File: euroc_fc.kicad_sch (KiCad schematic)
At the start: 147 parts, among them J1 Micro-Fit, J10 USB_C_Receptacle_USB2.0, J11 SWD Header, J2 Micro-Fit, J3 Micro-Fit, J4 SMA, J5 JST-GH, J6 JST-GH, J7 JST-GH, J9 Micro_SD_Card_Det, Q1 DMN2056U, Q2 AOSP21321, Q3 DMN2056U, Q4 AOSP21321, Q5 DMN2056U, SW1 EVQ-PUC02K, SW2 EVQ-PUC02K, U1 STM32F401RCT6, U10 Ai-Thinker-Ra-01, U11 W25Q256JVF, U12 MCP2517FD, U13 MCP2562-E-SN, U2 L7805, U3 L7805, U4 AZ1117I-3.3, U5 LSM6DSR, U6 H3LIS331DL, U7 MS5611-01BA, U8 LIS3MDL, U9 SAM-M8Q, Y1 25M, 18p, Y2 20M

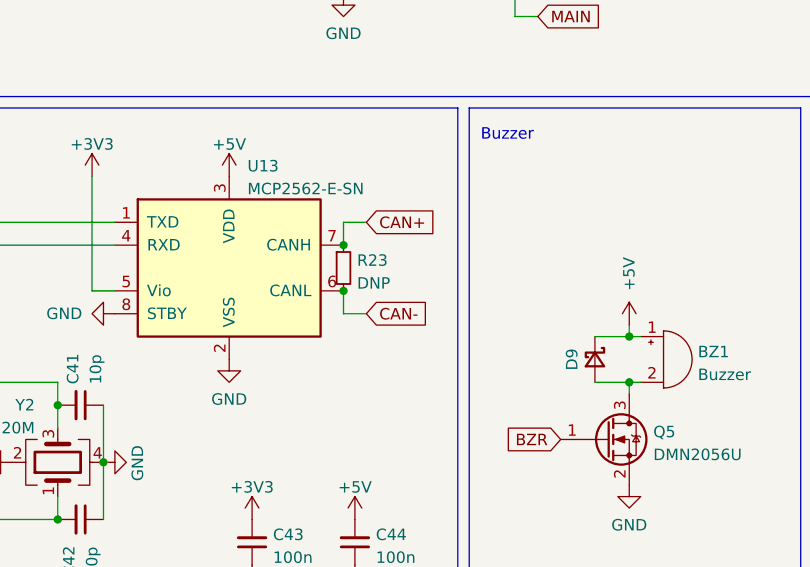
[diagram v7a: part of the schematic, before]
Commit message: Update BOM for rev. 2
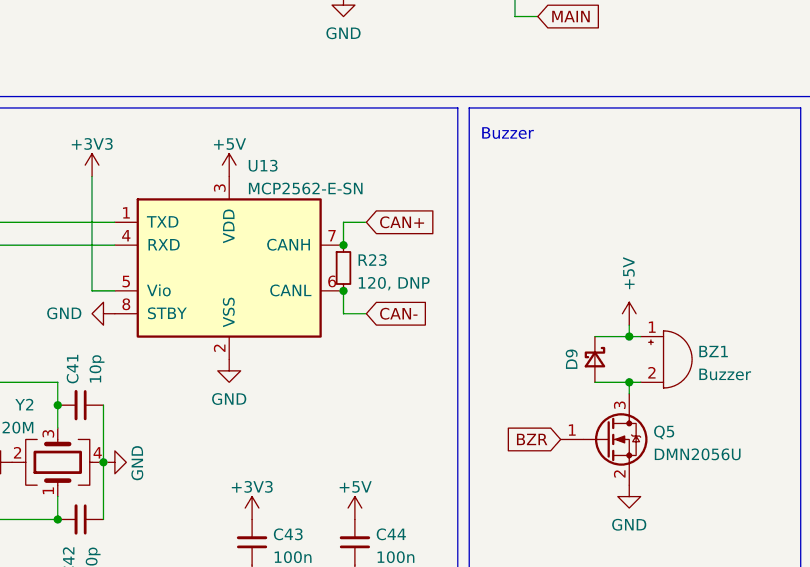
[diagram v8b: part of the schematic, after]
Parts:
- C41, C42: LCSC# (none) -> C1634; Manufacturer (none) -> Samsung Electro-Mechanics; Part# (none) -> CL10C100JB8NNNC
- J5, J6, J7: LCSC# (none) -> C189895; Manufacturer (none) -> JST; Part# (none) -> SM04B-GHS-TB
- R23: value DNP -> 120, DNP; LCSC# C22548 -> C114640; Part# RC0603FR-071KL -> RC0603FR-07120RL
- U11: LCSC# (none) -> C779876
- U12: DigiKey# (none) -> MCP2517FDT-H/SLCT-ND; Manufacturer (none) -> Microchip Technology; Part# (none) -> MCP2517FDT-H/SL
- U13: DigiKey# (none) -> MCP2562-H/SN; Manufacturer (none) -> Microchip Technology; Part# (none) -> MCP2562-H/SN
- U6: DigiKey# (none) -> 497-13903-1-ND; Manufacturer (none) -> STMicroelectronics; Part# (none) -> H3LIS331DLTR
- U8: DigiKey# (none) -> 497-13892-1-ND; LCSC# (none) -> C478483; Manufacturer (none) -> STMicroelectronics; Part# (none) -> LIS3MDLTR
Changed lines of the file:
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@@
       (effects (font (size 1.27 1.27)) hide)
     )
+    (property "Manufacturer" "Microchip Technology" (id 4) (at 173.99 148.59 0)
+      (effects (font (size 1.27 1.27)) hide)
+    )
+    (property "DigiKey#" "MCP2562-H/SN" (id 5) (at 173.99 148.59 0)
+      (effects (font (size 1.27 1.27)) hide)
+    )
+    (property "Part#" "MCP2562-H/SN" (id 6) (at 173.99 148.59 0)
+      (effects (font (size 1.27 1.27)) hide)
+    )
     (pin "1")
     (pin "2")
@@
       (effects (font (size 1.27 1.27)) (justify left))
     )
-    (property "Value" "DNP" (id 1) (at 188.1886 150.2922 0)
+    (property "Value" "120, DNP" (id 1) (at 188.1886 150.2922 0)
       (effects (font (size 1.27 1.27)) (justify left))
     )
@@
       (effects (font (size 1.27 1.27)) hide)
     )
-    (property "LCSC#" "C22548" (id 5) (at 186.69 148.59 0)
+    (property "LCSC#" "C114640" (id 5) (at 186.69 148.59 0)
       (effects (font (size 1.27 1.27)) hide)
     )
@@
       (effects (font (size 1.27 1.27)) hide)
     )
-    (property "Part#" "RC0603FR-071KL" (id 7) (at 186.69 148.59 0)
+    (property "Part#" "RC0603FR-07120RL" (id 7) (at 186.69 148.59 0)
       (effects (font (size 1.27 1.27)) hide)
     )
@@
       (effects (font (size 1.27 1.27)) hide)
     )
-    (property "LCSC#" "" (id 5) (at 157.48 176.53 0)
+    (property "LCSC#" "C1634" (id 5) (at 157.48 176.53 0)
       (effects (font (size 1.27 1.27)) hide)
     )
-    (property "Manufacturer" "" (id 6) (at 157.48 176.53 0)
+    (property "Manufacturer" "Samsung Electro-Mechanics" (id 6) (at 157.48 176.53 0)
       (effects (font (size 1.27 1.27)) hide)
     )
-    (property "Part#" "" (id 7) (at 157.48 176.53 0)
+    (property "Part#" "CL10C100JB8NNNC" (id 7) (at 157.48 176.53 0)
       (effects (font (size 1.27 1.27)) hide)
     )
@@
       (effects (font (size 1.27 1.27)) hide)
     )
-    (property "DigiKey#" "" (id 5) (at 80.01 83.82 0)
+    (property "DigiKey#" "497-13903-1-ND" (id 5) (at 80.01 83.82 0)
       (effects (font (size 1.27 1.27)) hide)
     )
-    (property "Manufacturer" "" (id 6) (at 80.01 83.82 0)
+    (property "Manufacturer" "STMicroelectronics" (id 6) (at 80.01 83.82 0)
       (effects (font (size 1.27 1.27)) hide)
     )
-    (property "Part#" "" (id 7) (at 80.01 83.82 0)
+    (property "Part#" "H3LIS331DLTR" (id 7) (at 80.01 83.82 0)
       (effects (font (size 1.27 1.27)) hide)
     )
@@
       (effects (font (size 1.27 1.27)) hide)
     )
+    (property "DigiKey#" "497-13892-1-ND" (id 4) (at 76.2 161.29 0)
+      (effects (font (size 1.27 1.27)) hide)
+    )
+    (property "LCSC#" "C478483" (id 5) (at 76.2 161.29 0)
+      (effects (font (size 1.27 1.27)) hide)
+    )
+    (property "Manufacturer" "STMicroelectronics" (id 6) (at 76.2 161.29 0)
+      (effects (font (size 1.27 1.27)) hide)
+    )
+    (property "Part#" "LIS3MDLTR" (id 7) (at 76.2 161.29 0)
+      (effects (font (size 1.27 1.27)) hide)
+    )
     (pin "1")
     (pin "10")
@@
       (effects (font (size 1.27 1.27)) hide)
     )
+    (property "LCSC#" "C779876" (id 8) (at 149.86 254 0)
+      (effects (font (size 1.27 1.27)) hide)
+    )
     (pin "1")
     (pin "10")
@@
       (effects (font (size 1.27 1.27)) hide)
     )
+    (property "LCSC#" "C189895" (id 4) (at 125.73 208.28 0)
+      (effects (font (size 1.27 1.27)) hide)
+    )
+    (property "Manufacturer" "JST" (id 5) (at 125.73 208.28 0)
+      (effects (font (size 1.27 1.27)) hide)
+    )
+    (property "Part#" "SM04B-GHS-TB" (id 6) (at 125.73 208.28 0)
+      (effects (font (size 1.27 1.27)) hide)
+    )
     (pin "1")
     (pin "2")
@@
       (effects (font (size 1.27 1.27)) hide)
     )
+    (property "LCSC#" "C189895" (id 4) (at 182.88 208.28 0)
+      (effects (font (size 1.27 1.27)) hide)
+    )
+    (property "Manufacturer" "JST" (id 5) (at 182.88 208.28 0)
+      (effects (font (size 1.27 1.27)) hide)
+    )
+    (property "Part#" "SM04B-GHS-TB" (id 6) (at 182.88 208.28 0)
+      (effects (font (size 1.27 1.27)) hide)
+    )
     (pin "1")
     (pin "2")
@@
       (effects (font (size 1.27 1.27)) hide)
     )
+    (property "LCSC#" "C189895" (id 4) (at 158.75 208.28 0)
+      (effects (font (size 1.27 1.27)) hide)
+    )
+    (property "Manufacturer" "JST" (id 5) (at 158.75 208.28 0)
+      (effects (font (size 1.27 1.27)) hide)
+    )
+    (property "Part#" "SM04B-GHS-TB" (id 6) (at 158.75 208.28 0)
+      (effects (font (size 1.27 1.27)) hide)
+    )
     (pin "1")
     (pin "2")
@@
       (effects (font (size 1.27 1.27)) hide)
     )
-    (property "LCSC#" "" (id 5) (at 157.48 163.83 0)
+    (property "LCSC#" "C1634" (id 5) (at 157.48 163.83 0)
       (effects (font (size 1.27 1.27)) hide)
     )
-    (property "Manufacturer" "" (id 6) (at 157.48 163.83 0)
+    (property "Manufacturer" "Samsung Electro-Mechanics" (id 6) (at 157.48 163.83 0)
       (effects (font (size 1.27 1.27)) hide)
     )
-    (property "Part#" "" (id 7) (at 157.48 163.83 0)
+    (property "Part#" "CL10C100JB8NNNC" (id 7) (at 157.48 163.83 0)
       (effects (font (size 1.27 1.27)) hide)
     )
@@
       (effects (font (size 1.27 1.27)) hide)
     )
+    (property "Manufacturer" "Microchip Technology" (id 4) (at 132.08 153.67 0)
+      (effects (font (size 1.27 1.27)) hide)
+    )
+    (property "DigiKey#" "MCP2517FDT-H/SLCT-ND" (id 5) (at 132.08 153.67 0)
+      (effects (font (size 1.27 1.27)) hide)
+    )
+    (property "Part#" "MCP2517FDT-H/SL" (id 6) (at 132.08 153.67 0)
+      (effects (font (size 1.27 1.27)) hide)
+    )
     (pin "1")
     (pin "10")
@@
     )
     (path "/0dfb1a29-a10a-4b51-bd36-e4639a1bc660"
-      (reference "R23") (unit 1) (value "DNP") (footprint "Resistor_SMD:R_0603_1608Metric")
+      (reference "R23") (unit 1) (value "120, DNP") (footprint "Resistor_SMD:R_0603_1608Metric")
     )
     (path "/41ee0fa9-5d54-4e7c-b416-7989d4fd4d68"
